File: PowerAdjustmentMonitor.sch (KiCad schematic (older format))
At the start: 36 parts, among them U3 LM317T, U4 LM317T, U5 LM337T, U6 LM337T

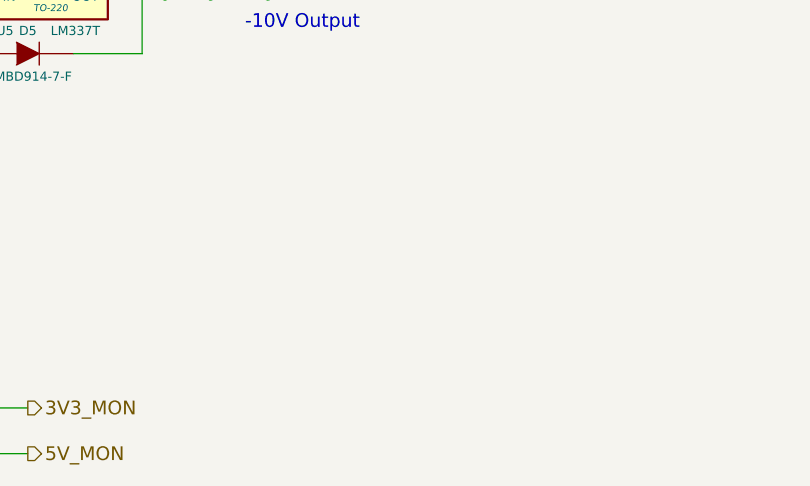
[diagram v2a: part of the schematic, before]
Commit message: More small tweaks (cf. Layout Work Session 16)
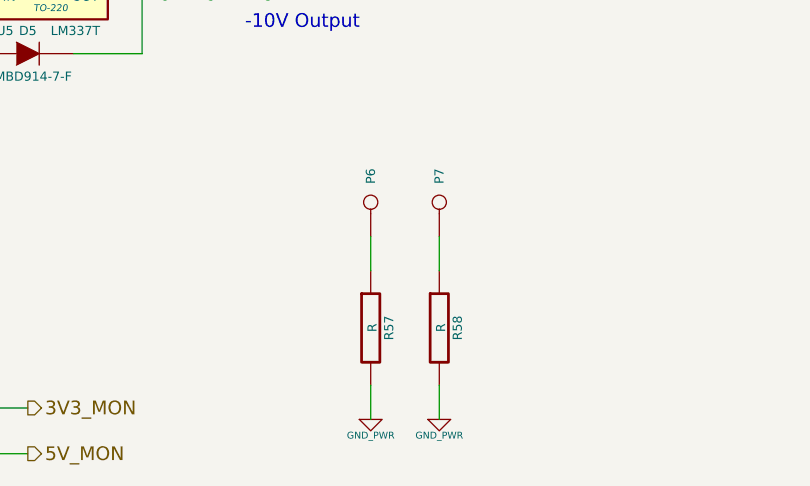
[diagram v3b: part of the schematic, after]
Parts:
- added P6, P7: CONN_1, symbol CONN_1
- added R57, R58: R, symbol R
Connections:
- net GND_PWR: now also R57.2, R58.2
- new net: P6.1, R57.1
- new net: P7.1, R58.1
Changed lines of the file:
@@
 $EndDescr
 $Comp
-L +3.3V #PWR028
+L +3.3V #PWR36
 U 1 1 52F2A379
 P 2200 6200
-F 0 "#PWR028" H 2200 6160 30  0001 C CNN
+F 0 "#PWR36" H 2200 6160 30  0001 C CNN
 F 1 "+3.3V" H 2200 6310 30  0000 C CNN
 F 2 "" H 2200 6200 60  0000 C CNN
@@
 $EndComp
 $Comp
-L +5V #PWR029
+L +5V #PWR35
 U 1 1 52F2A37F
 P 2000 6200
-F 0 "#PWR029" H 2000 6290 20  0001 C CNN
+F 0 "#PWR35" H 2000 6290 20  0001 C CNN
 F 1 "+5V" H 2000 6290 30  0000 C CNN
 F 2 "" H 2000 6200 60  0000 C CNN
@@
 $EndComp
 $Comp
-L +12V #PWR030
+L +12V #PWR32
 U 1 1 52F2A40B
 P 1700 1700
-F 0 "#PWR030" H 1700 1650 20  0001 C CNN
+F 0 "#PWR32" H 1700 1650 20  0001 C CNN
 F 1 "+12V" H 1700 1800 30  0000 C CNN
 F 2 "" H 1700 1700 60  0000 C CNN
@@
 $EndComp
 $Comp
-L -12V #PWR031
+L -12V #PWR34
 U 1 1 52F2A411
 P 1700 4700
-F 0 "#PWR031" H 1700 4830 20  0001 C CNN
+F 0 "#PWR34" H 1700 4830 20  0001 C CNN
 F 1 "-12V" H 1700 4800 30  0000 C CNN
 F 2 "" H 1700 4700 60  0000 C CNN
@@
 $EndComp
 $Comp
-L FE_V+ #PWR032
+L FE_V+ #PWR37
 U 1 1 52F2A802
 P 4100 1700
-F 0 "#PWR032" H 4100 1800 30  0001 C CNN
+F 0 "#PWR37" H 4100 1800 30  0001 C CNN
 F 1 "FE_V+" H 4100 1800 30  0000 C CNN
 F 2 "" H 4100 1700 60  0000 C CNN
@@
 $EndComp
 $Comp
-L GND_PWR #PWR033
+L GND_PWR #PWR42
 U 1 1 53152874
 P 5600 3550
-F 0 "#PWR033" H 5600 3550 30  0001 C CNN
+F 0 "#PWR42" H 5600 3550 30  0001 C CNN
 F 1 "GND_PWR" H 5600 3480 30  0000 C CNN
 F 2 "" H 5600 3550 60  0000 C CNN
@@
 $EndComp
 $Comp
-L +12V #PWR034
+L +12V #PWR41
 U 1 1 5315289E
 P 5600 1750
-F 0 "#PWR034" H 5600 1700 20  0001 C CNN
+F 0 "#PWR41" H 5600 1700 20  0001 C CNN
 F 1 "+12V" H 5600 1850 30  0000 C CNN
 F 2 "" H 5600 1750 60  0000 C CNN
@@
 $EndComp
 $Comp
-L -12V #PWR035
+L -12V #PWR43
 U 1 1 53152B82
 P 5600 4700
-F 0 "#PWR035" H 5600 4830 20  0001 C CNN
+F 0 "#PWR43" H 5600 4830 20  0001 C CNN
 F 1 "-12V" H 5600 4800 30  0000 C CNN
 F 2 "" H 5600 4700 60  0000 C CNN
@@
 Connection ~ 8700 3400
 $Comp
-L AGND #PWR036
+L AGND #PWR33
 U 1 1 5316392A
 P 1700 3600
-F 0 "#PWR036" H 1700 3600 40  0001 C CNN
+F 0 "#PWR33" H 1700 3600 40  0001 C CNN
 F 1 "AGND" H 1700 3530 50  0000 C CNN
 F 2 "" H 1700 3600 60  0000 C CNN
@@
 Wire Wire Line
 	6700 4200 7550 4200
+$Comp
+L R R57
+U 1 1 5320E898
+P 4200 6350
+F 0 "R57" V 4280 6350 40  0000 C CNN
+F 1 "R" V 4207 6351 40  0000 C CNN
+F 2 "" V 4130 6350 30  0000 C CNN
+F 3 "" H 4200 6350 30  0000 C CNN
+	1    4200 6350
+	1    0    0    -1
+$EndComp
+$Comp
+L GND_PWR #PWR39
+U 1 1 5320E8AA
+P 4200 6750
+F 0 "#PWR39" H 4200 6750 30  0001 C CNN
+F 1 "GND_PWR" H 4200 6680 30  0000 C CNN
+F 2 "" H 4200 6750 60  0000 C CNN
+F 3 "" H 4200 6750 60  0000 C CNN
+	1    4200 6750
+	1    0    0    -1
+$EndComp
+Wire Wire Line
+	4200 6600 4200 6750
+$Comp
+L CONN_1 P6
+U 1 1 5320E8B6
+P 4200 5800
+F 0 "P6" H 4280 5800 40  0000 L CNN
+F 1 "CONN_1" H 4200 5855 30  0001 C CNN
+F 2 "" H 4200 5800 60  0000 C CNN
+F 3 "" H 4200 5800 60  0000 C CNN
+	1    4200 5800
+	0    -1   -1   0
+$EndComp
+Wire Wire Line
+	4200 5950 4200 6100
+$Comp
+L R R58
+U 1 1 5320E9DD
+P 4500 6350
+F 0 "R58" V 4580 6350 40  0000 C CNN
+F 1 "R" V 4507 6351 40  0000 C CNN
+F 2 "" V 4430 6350 30  0000 C CNN
+F 3 "" H 4500 6350 30  0000 C CNN
+	1    4500 6350
+	1    0    0    -1
+$EndComp
+$Comp
+L GND_PWR #PWR40
+U 1 1 5320E9E3
+P 4500 6750
+F 0 "#PWR40" H 4500 6750 30  0001 C CNN
+F 1 "GND_PWR" H 4500 6680 30  0000 C CNN
+F 2 "" H 4500 6750 60  0000 C CNN
+F 3 "" H 4500 6750 60  0000 C CNN
+	1    4500 6750
+	1    0    0    -1
+$EndComp
+Wire Wire Line
+	4500 6600 4500 6750
+$Comp
+L CONN_1 P7
+U 1 1 5320E9EA
+P 4500 5800
+F 0 "P7" H 4580 5800 40  0000 L CNN
+F 1 "CONN_1" H 4500 5855 30  0001 C CNN
+F 2 "" H 4500 5800 60  0000 C CNN
+F 3 "" H 4500 5800 60  0000 C CNN
+	1    4500 5800
+	0    -1   -1   0
+$EndComp
+Wire Wire Line
+	4500 5950 4500 6100
 $EndSCHEMATC

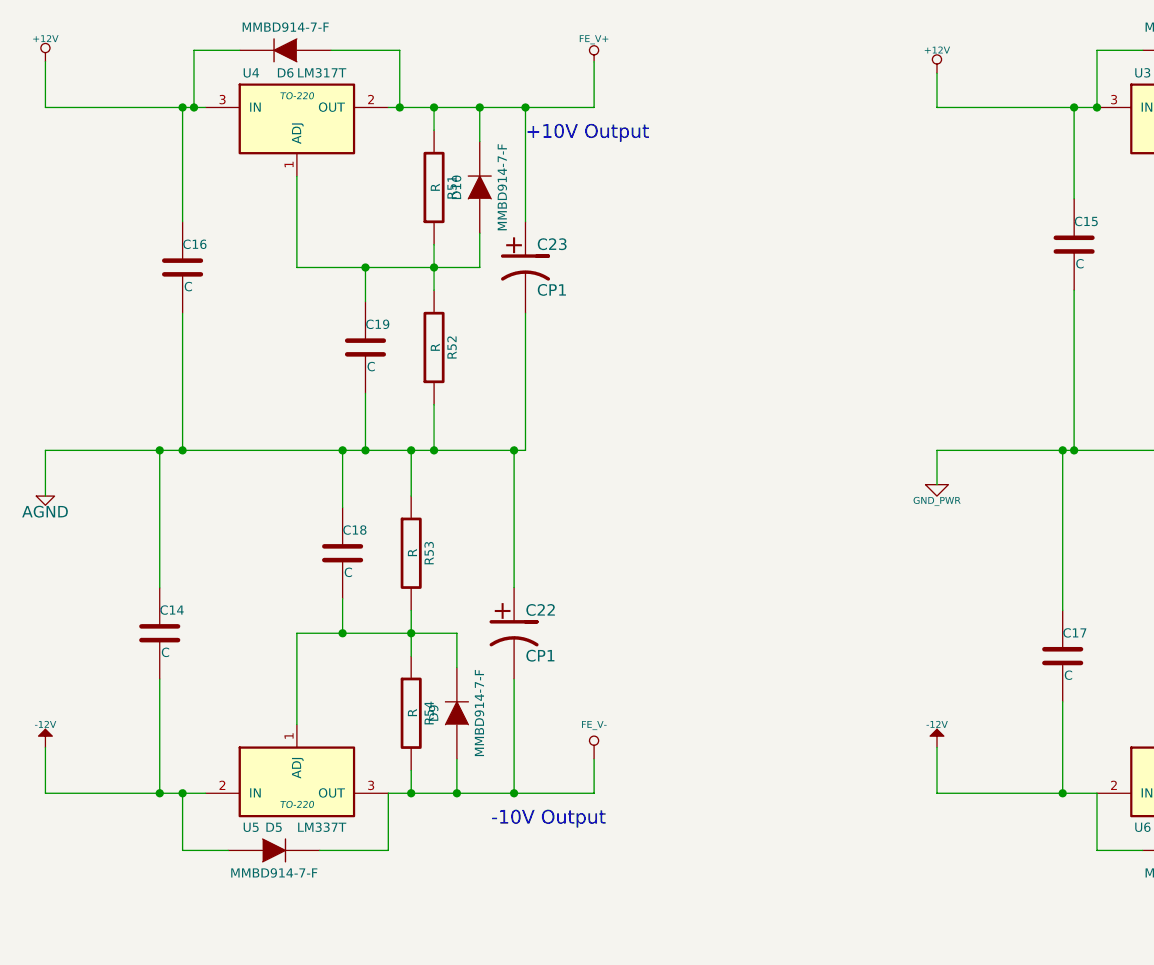
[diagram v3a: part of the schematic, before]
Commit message: Test points added, silk screen updates
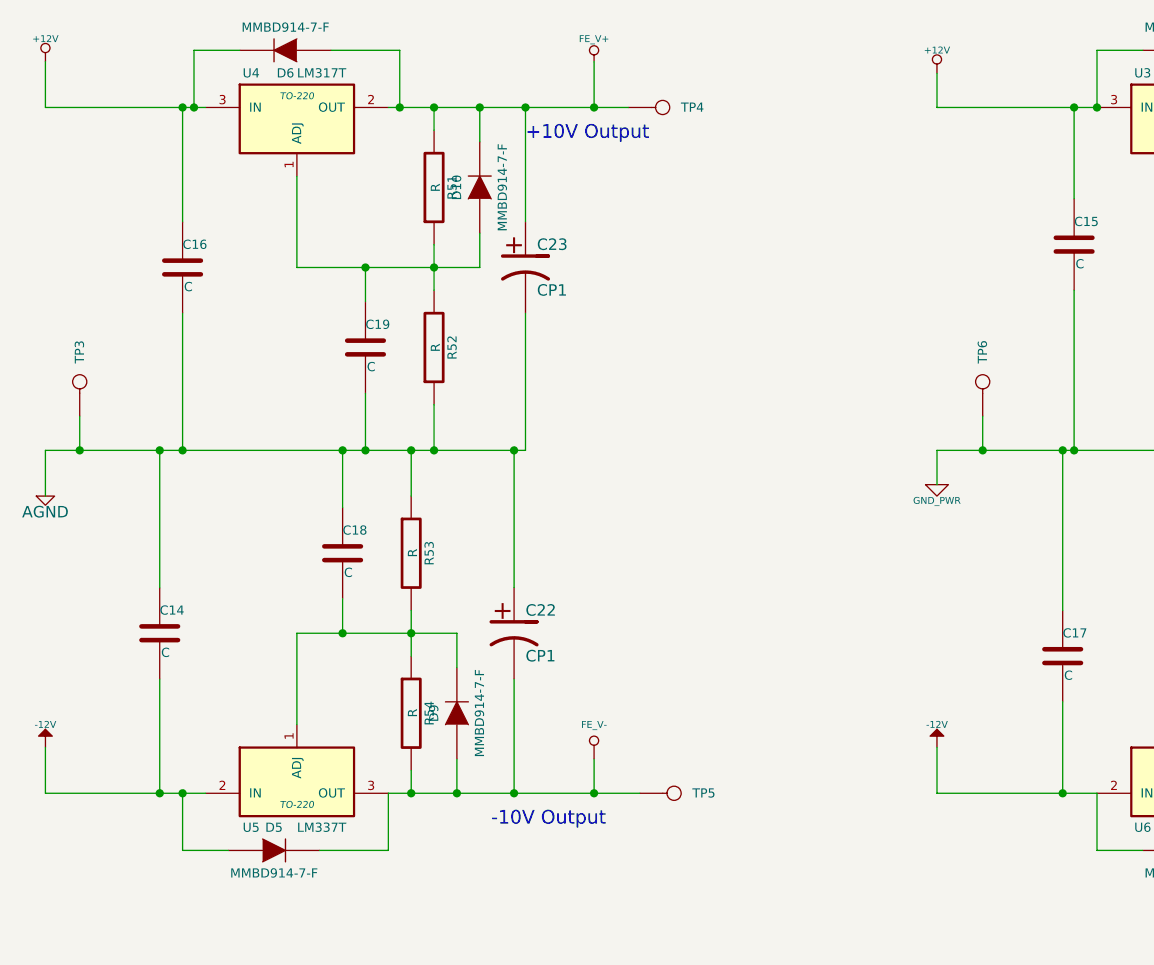
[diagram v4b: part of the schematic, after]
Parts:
- added TP3: AGND, symbol CONN_1
- added TP4: FE_V+, symbol CONN_1
- added TP5: FE_V-, symbol CONN_1
- added TP6: GND_PWR, symbol CONN_1
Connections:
- net AGND: now also TP3.1
- net FE_V+: now also TP4.1
- net FE_V-: now also TP5.1
- net GND_PWR: now also TP6.1
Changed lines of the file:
@@
 $EndDescr
 $Comp
-L +3.3V #PWR36
+L +3.3V #PWR028
 U 1 1 52F2A379
 P 2200 6200
-F 0 "#PWR36" H 2200 6160 30  0001 C CNN
+F 0 "#PWR028" H 2200 6160 30  0001 C CNN
 F 1 "+3.3V" H 2200 6310 30  0000 C CNN
 F 2 "" H 2200 6200 60  0000 C CNN
@@
 $EndComp
 $Comp
-L +5V #PWR35
+L +5V #PWR029
 U 1 1 52F2A37F
 P 2000 6200
-F 0 "#PWR35" H 2000 6290 20  0001 C CNN
+F 0 "#PWR029" H 2000 6290 20  0001 C CNN
 F 1 "+5V" H 2000 6290 30  0000 C CNN
 F 2 "" H 2000 6200 60  0000 C CNN
@@
 $EndComp
 $Comp
-L +12V #PWR32
+L +12V #PWR030
 U 1 1 52F2A40B
 P 1700 1700
-F 0 "#PWR32" H 1700 1650 20  0001 C CNN
+F 0 "#PWR030" H 1700 1650 20  0001 C CNN
 F 1 "+12V" H 1700 1800 30  0000 C CNN
 F 2 "" H 1700 1700 60  0000 C CNN
@@
 $EndComp
 $Comp
-L -12V #PWR34
+L -12V #PWR031
 U 1 1 52F2A411
 P 1700 4700
-F 0 "#PWR34" H 1700 4830 20  0001 C CNN
+F 0 "#PWR031" H 1700 4830 20  0001 C CNN
 F 1 "-12V" H 1700 4800 30  0000 C CNN
 F 2 "" H 1700 4700 60  0000 C CNN
@@
 $EndComp
 $Comp
-L FE_V+ #PWR37
+L FE_V+ #PWR032
 U 1 1 52F2A802
 P 4100 1700
-F 0 "#PWR37" H 4100 1800 30  0001 C CNN
+F 0 "#PWR032" H 4100 1800 30  0001 C CNN
 F 1 "FE_V+" H 4100 1800 30  0000 C CNN
 F 2 "" H 4100 1700 60  0000 C CNN
@@
 $EndComp
 $Comp
-L GND_PWR #PWR42
+L GND_PWR #PWR033
 U 1 1 53152874
 P 5600 3550
-F 0 "#PWR42" H 5600 3550 30  0001 C CNN
+F 0 "#PWR033" H 5600 3550 30  0001 C CNN
 F 1 "GND_PWR" H 5600 3480 30  0000 C CNN
 F 2 "" H 5600 3550 60  0000 C CNN
@@
 $EndComp
 $Comp
-L +12V #PWR41
+L +12V #PWR034
 U 1 1 5315289E
 P 5600 1750
-F 0 "#PWR41" H 5600 1700 20  0001 C CNN
+F 0 "#PWR034" H 5600 1700 20  0001 C CNN
 F 1 "+12V" H 5600 1850 30  0000 C CNN
 F 2 "" H 5600 1750 60  0000 C CNN
@@
 $EndComp
 $Comp
-L -12V #PWR43
+L -12V #PWR035
 U 1 1 53152B82
 P 5600 4700
-F 0 "#PWR43" H 5600 4830 20  0001 C CNN
+F 0 "#PWR035" H 5600 4830 20  0001 C CNN
 F 1 "-12V" H 5600 4800 30  0000 C CNN
 F 2 "" H 5600 4700 60  0000 C CNN
@@
 	1700 1900 1700 1700
 Wire Wire Line
-	3200 1900 4100 1900
+	3200 1900 4250 1900
 Wire Wire Line
 	4100 1900 4100 1700
@@
 Connection ~ 8700 1900
 Wire Wire Line
-	3200 4900 4100 4900
+	3200 4900 4300 4900
 Connection ~ 3300 4900
 Wire Wire Line
@@
 Connection ~ 8700 3400
 $Comp
-L AGND #PWR33
+L AGND #PWR036
 U 1 1 5316392A
 P 1700 3600
-F 0 "#PWR33" H 1700 3600 40  0001 C CNN
+F 0 "#PWR036" H 1700 3600 40  0001 C CNN
 F 1 "AGND" H 1700 3530 50  0000 C CNN
 F 2 "" H 1700 3600 60  0000 C CNN
@@
 $EndComp
 $Comp
-L GND_PWR #PWR39
+L GND_PWR #PWR037
 U 1 1 5320E8AA
 P 4200 6750
-F 0 "#PWR39" H 4200 6750 30  0001 C CNN
+F 0 "#PWR037" H 4200 6750 30  0001 C CNN
 F 1 "GND_PWR" H 4200 6680 30  0000 C CNN
 F 2 "" H 4200 6750 60  0000 C CNN
@@
 $EndComp
 $Comp
-L GND_PWR #PWR40
+L GND_PWR #PWR038
 U 1 1 5320E9E3
 P 4500 6750
-F 0 "#PWR40" H 4500 6750 30  0001 C CNN
+F 0 "#PWR038" H 4500 6750 30  0001 C CNN
 F 1 "GND_PWR" H 4500 6680 30  0000 C CNN
 F 2 "" H 4500 6750 60  0000 C CNN
@@
 Wire Wire Line
 	4500 5950 4500 6100
+$Comp
+L CONN_1 TP4
+U 1 1 53224C20
+P 4400 1900
+F 0 "TP4" H 4480 1900 40  0000 L CNN
+F 1 "FE_V+" H 4400 1955 30  0001 C CNN
+F 2 "" H 4400 1900 60  0000 C CNN
+F 3 "" H 4400 1900 60  0000 C CNN
+	1    4400 1900
+	1    0    0    -1
+$EndComp
+$Comp
+L CONN_1 TP6
+U 1 1 53224C2B
+P 5800 3100
+F 0 "TP6" H 5880 3100 40  0000 L CNN
+F 1 "GND_PWR" H 5800 3155 30  0001 C CNN
+F 2 "" H 5800 3100 60  0000 C CNN
+F 3 "" H 5800 3100 60  0000 C CNN
+	1    5800 3100
+	0    -1   -1   0
+$EndComp
+Wire Wire Line
+	5800 3250 5800 3400
+Connection ~ 5800 3400
+Connection ~ 4100 1900
+$Comp
+L CONN_1 TP5
+U 1 1 53224D8E
+P 4450 4900
+F 0 "TP5" H 4530 4900 40  0000 L CNN
+F 1 "FE_V-" H 4450 4955 30  0001 C CNN
+F 2 "" H 4450 4900 60  0000 C CNN
+F 3 "" H 4450 4900 60  0000 C CNN
+	1    4450 4900
+	1    0    0    -1
+$EndComp
+Connection ~ 4100 4900
+$Comp
+L CONN_1 TP3
+U 1 1 53224E47
+P 1850 3100
+F 0 "TP3" H 1930 3100 40  0000 L CNN
+F 1 "AGND" H 1850 3155 30  0001 C CNN
+F 2 "" H 1850 3100 60  0000 C CNN
+F 3 "" H 1850 3100 60  0000 C CNN
+	1    1850 3100
+	0    -1   -1   0
+$EndComp
+Wire Wire Line
+	1850 3250 1850 3400
+Connection ~ 1850 3400
 $EndSCHEMATC

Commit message: Added some R/C to analog sections
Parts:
- removed TP4: FE_V+, symbol CONN_1
- removed TP5: FE_V-, symbol CONN_1
- added K2, K3: CONN_3, symbol CONN_3
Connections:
- net +12V: now also K3.2 (PM); no longer D6.2 (K), U4.3 (IN)
- net -12V: now also K2.2 (PM); no longer D5.1 (A), U5.2 (IN)
- net FE_V+: now also K3.3 (P3)
- net FE_V-: now also K2.3 (P3)
- new net: D6.2 (K), K3.1 (P1), U4.3 (IN)
- new net: D5.1 (A), K2.1 (P1), U5.2 (IN)
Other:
- moved on the sheet: C14, C16, P6, P7, R57, R58, TP3
